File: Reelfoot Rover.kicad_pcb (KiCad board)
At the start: 2 copper layers, 65 x 56 mm, 30 parts, among them J1 GPIO, J10 FR Motor, J11 RL Motor, J12 RR Motor, J2 HC-SR04 1, J3 HC-SR04 2, J4 HC-SR04 3, J5 Encoder 1, J6 Encoder 2, J7 Encoder 3, J8 Encoder 4, J9 FL Motor, U1 L293D, U2 L293D, U3 7432

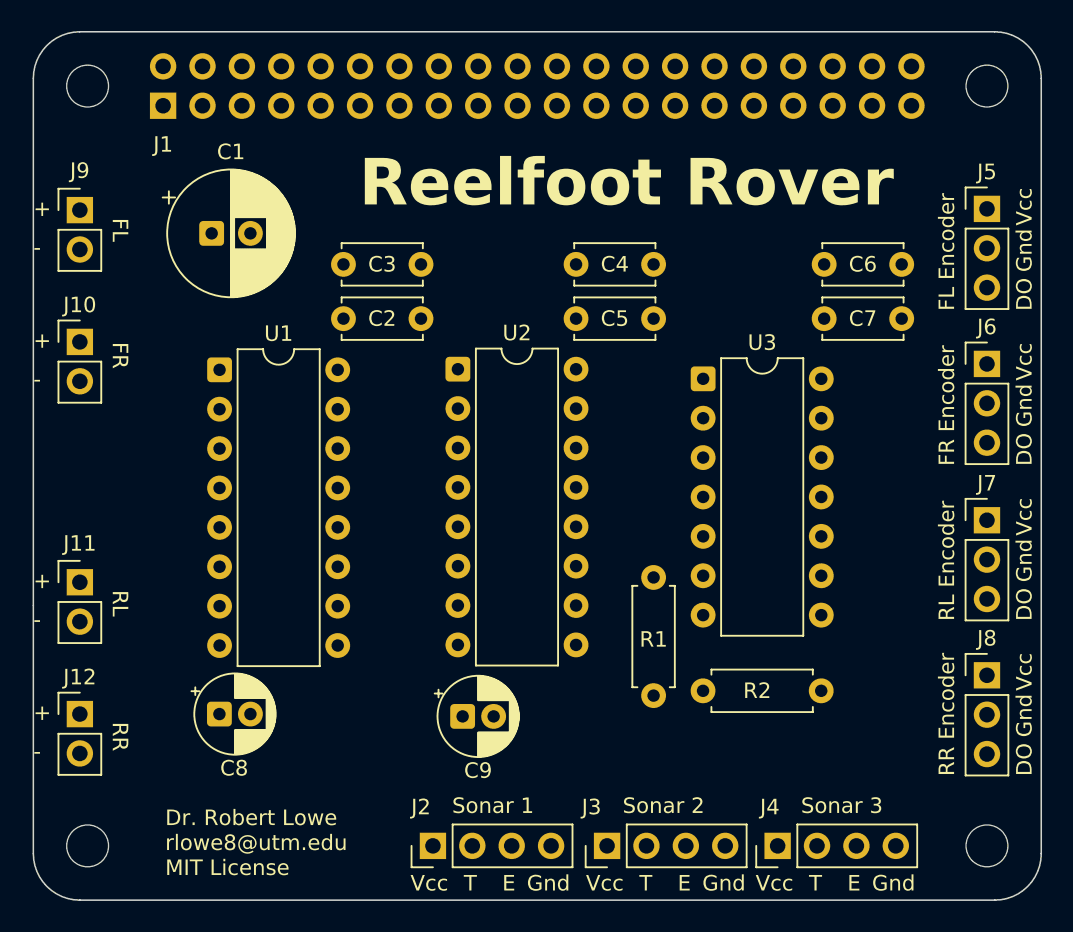
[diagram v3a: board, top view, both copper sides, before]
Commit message: Routing more connections
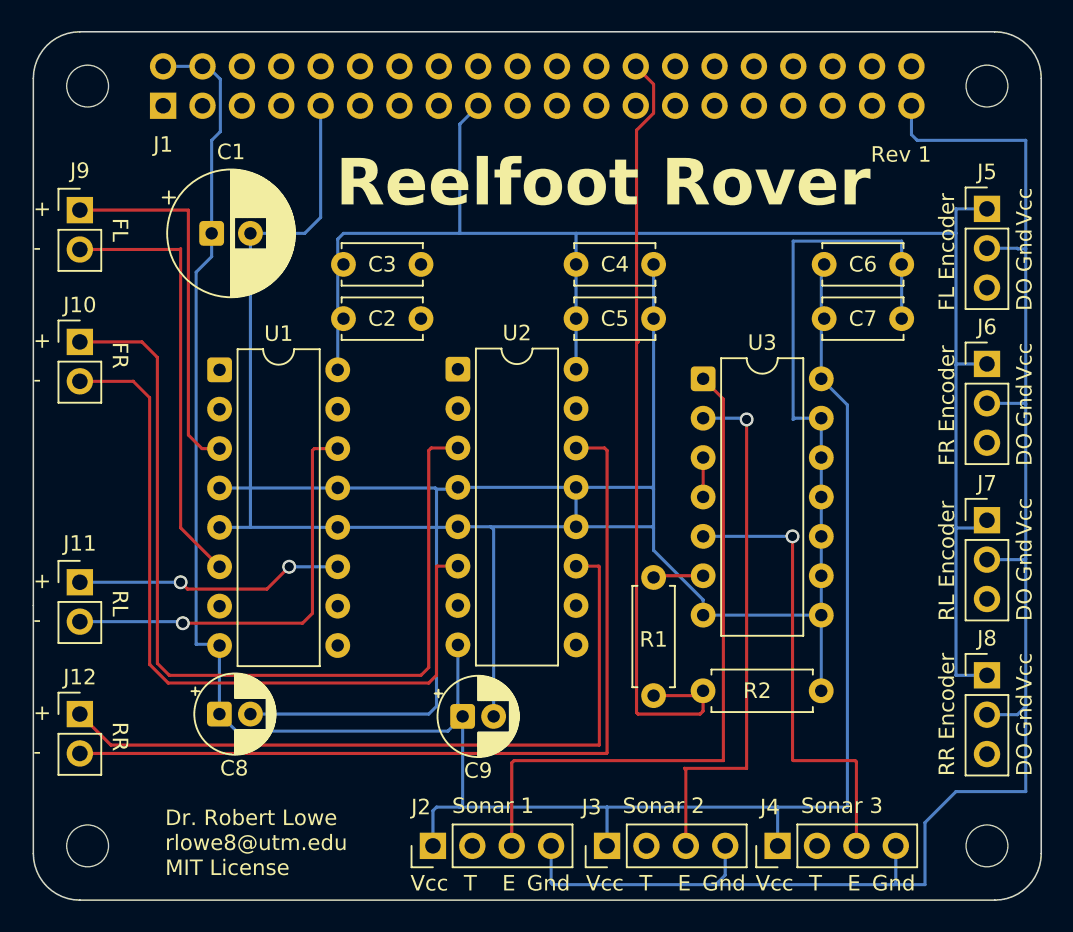
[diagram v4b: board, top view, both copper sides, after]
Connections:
- U2 pad 9: FR Enable -> RR Enable
- U3 pad 5: SO Echo 2 -> SO Echo 3
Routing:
- net GND: track 0.00 -> 307.7 mm
- net 5V: track 0.00 -> 144.2 mm
- net 3V3: track 0.00 -> 104.3 mm
- net FR+: track 0.00 -> 59.1 mm
- net RR-: track 0.00 -> 55.6 mm
- net SO Echo: track 0.00 -> 51.7 mm
- net FR-: track 0.00 -> 49.7 mm
- net RR+: track 0.00 -> 47.3 mm
- net SO Echo 1: track 0.00 -> 44.2 mm
- net SO Echo 2: track 0.00 -> 34.4 mm, vias 0 -> 1
- net SO Echo 3: track 0.00 -> 30.4 mm, vias 0 -> 1
- net FL-: track 0.00 -> 28.1 mm
- net RL-: track 0.00 -> 27.5 mm, vias 0 -> 1
- net FL+: track 0.00 -> 23.9 mm
- net RL+: track 0.00 -> 17.4 mm, vias 0 -> 2
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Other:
- board text added: "Rev 1"

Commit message: More Routing!
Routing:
- net FR Enc: track 0.00 -> 184.0 mm
- net FL Enc: track 0.00 -> 149.1 mm
- net FR ML2: track 0.00 -> 119.4 mm
- net SO Trig 3: track 0.00 -> 101.4 mm
- net SO Trig 2: track 0.00 -> 101.0 mm
- net 3V3: track 104.3 -> 205.0 mm, vias 0 -> 1
- net SO Trig 1: track 0.00 -> 87.1 mm
- net RL Enable: track 0.00 -> 81.7 mm
- net FL ML2: track 0.00 -> 73.9 mm
- net RR Enable: track 0.00 -> 61.1 mm
- net GND: track 307.7 -> 354.4 mm
- net FL ML1: track 0.00 -> 45.7 mm
- net FR Enable: track 0.00 -> 42.9 mm, vias 0 -> 1
- net RR ML1: track 0.00 -> 40.1 mm, vias 0 -> 1
- net RL ML2: track 0.00 -> 39.1 mm
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
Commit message: Completed traces
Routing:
- net RR Enc: track 0.00 -> 92.1 mm, vias 0 -> 6
- net RL Enc: track 0.00 -> 76.5 mm
- net RR ML2: track 0.00 -> 75.5 mm, vias 0 -> 2
- net FL Enable: track 0.00 -> 69.9 mm, vias 0 -> 6
- net RL ML1: track 0.00 -> 40.6 mm, vias 0 -> 2
- net GND: track 354.4 -> 350.3 mm
- net 3V3: track 205.0 -> 206.9 mm
